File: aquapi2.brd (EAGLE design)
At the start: 102.5 x 80 mm, 4 parts, among them IC1 RASPBERRY_PI_ZERO_W__V1.3_

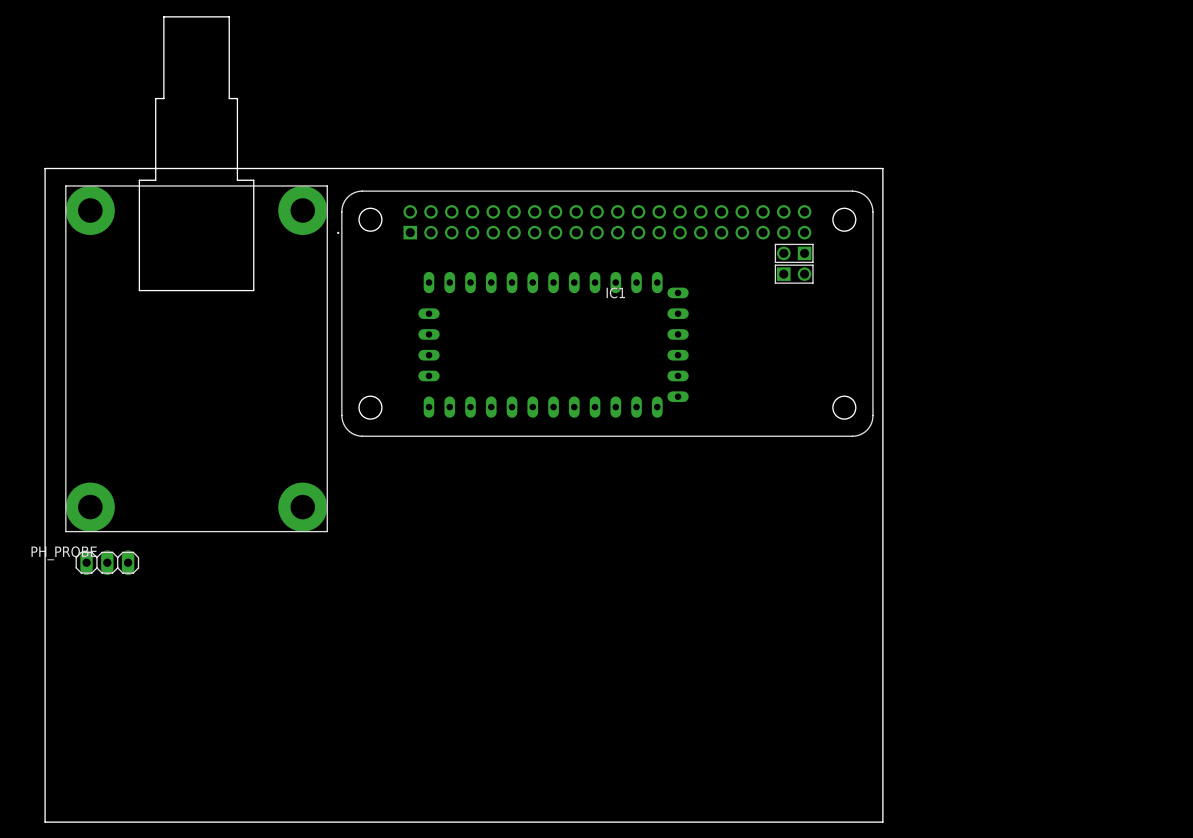
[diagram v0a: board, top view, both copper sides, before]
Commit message: relayx8 lib added
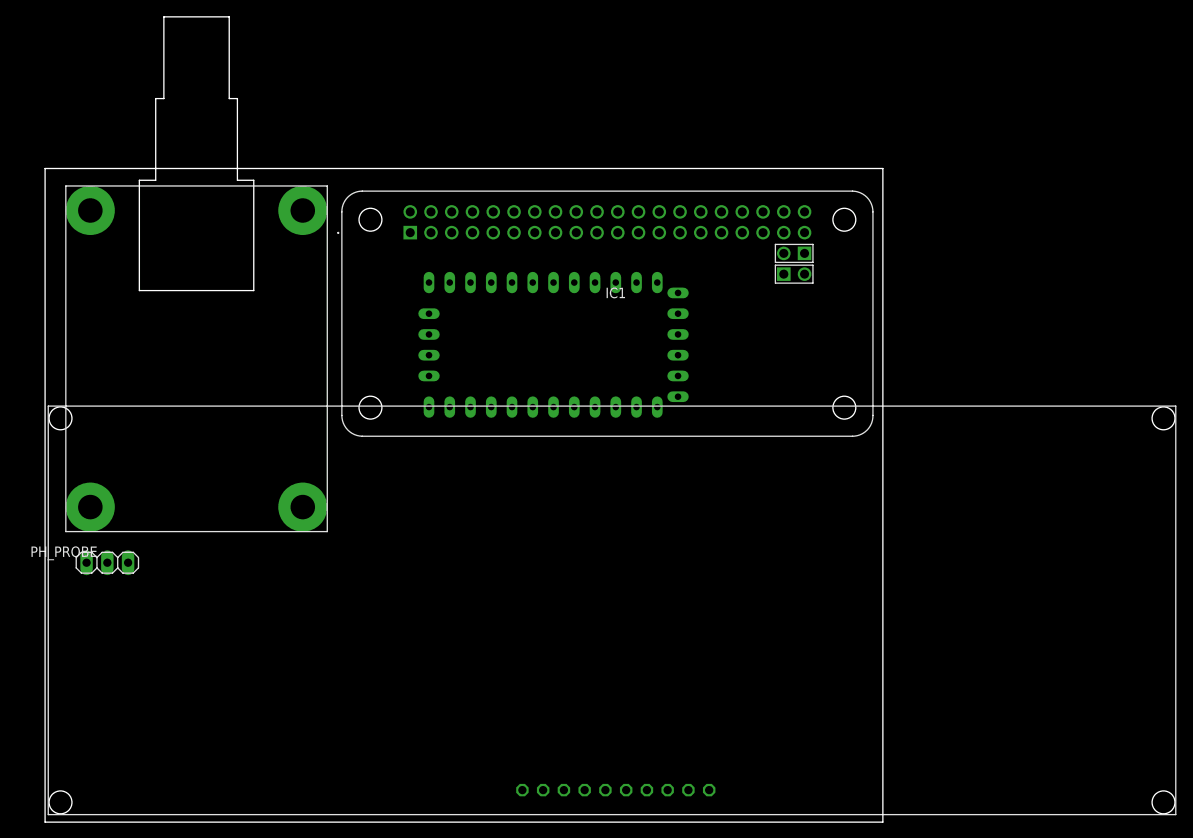
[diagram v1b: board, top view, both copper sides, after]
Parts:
- added U$3: RELAY_X8, RELAYx8:RELAY_X8
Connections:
- net +5V: now also U$3.VCC
- net GND: now also U$3.GND
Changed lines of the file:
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@@
 <setting verticaltext="up"/>
 </settings>
-<grid distance="50" unitdist="mil" unit="mil" style="lines" multiple="1" display="no" altdistance="5" altunitdist="mil" altunit="mil"/>
+<grid distance="1" unitdist="mm" unit="mm" style="lines" multiple="1" display="no" altdistance="1" altunitdist="mil" altunit="mm"/>
 <layers>
 <layer number="1" name="Top" color="4" fill="1" visible="yes" active="yes"/>
@@
 <attribute name="VALUE" x="11.43" y="34.925" size="1.27" layer="27" rot="R180"/>
 </element>
+<element name="U$3" library="RELAYx8" package="RELAY_X8" value="RELAY_X8" x="0.39" y="0.92" smashed="yes"/>
 </elements>
 <signals>
@@
 <contactref element="U$2" pad="GND"/>
 <contactref element="IC1" pad="14"/>
+<contactref element="U$3" pad="GND"/>
 <wire x1="85.335" y1="74.69" x2="92.955" y2="72.15" width="0" layer="19" extent="1-1"/>
 <wire x1="80.255" y1="74.69" x2="85.335" y2="74.69" width="0" layer="19" extent="1-1"/>
 <wire x1="75.175" y1="72.15" x2="80.255" y2="74.69" width="0" layer="19" extent="1-1"/>
+<wire x1="77.47" y1="64.77" x2="75.175" y2="72.15" width="0" layer="19" extent="1-1"/>
+<wire x1="77.47" y1="62.23" x2="77.47" y2="64.77" width="0" layer="19" extent="1-1"/>
 <wire x1="67.555" y1="74.69" x2="75.175" y2="72.15" width="0" layer="19" extent="1-1"/>
 <wire x1="59.935" y1="74.69" x2="67.555" y2="74.69" width="0" layer="19" extent="1-1"/>
-<wire x1="72.39" y1="50.8" x2="59.935" y2="74.69" width="0" layer="19" extent="1-1"/>
-<wire x1="77.47" y1="62.23" x2="72.39" y2="50.8" width="0" layer="19" extent="1-1"/>
-<wire x1="77.47" y1="64.77" x2="77.47" y2="62.23" width="0" layer="19" extent="1-1"/>
-<wire x1="67.31" y1="66.04" x2="77.47" y2="64.77" width="0" layer="19" extent="1-1"/>
-<wire x1="5.08" y1="31.75" x2="67.31" y2="66.04" width="0" layer="19" extent="1-1"/>
+<wire x1="67.31" y1="66.04" x2="67.555" y2="74.69" width="0" layer="19" extent="1-1"/>
+<wire x1="72.39" y1="50.8" x2="77.47" y2="62.23" width="0" layer="19" extent="1-1"/>
+<wire x1="5.08" y1="31.75" x2="59.935" y2="74.69" width="0" layer="19" extent="1-1"/>
+<wire x1="58.42" y1="3.92" x2="5.08" y2="31.75" width="0" layer="19" extent="1-1"/>
 </signal>
 <signal name="+5V">
@@
 <contactref element="IC1" pad="4"/>
 <contactref element="U$2" pad="VCC"/>
+<contactref element="U$3" pad="VCC"/>
 <wire x1="44.695" y1="74.69" x2="47.235" y2="74.69" width="0" layer="19" extent="1-1"/>
-<wire x1="67.31" y1="50.8" x2="44.695" y2="74.69" width="0" layer="19" extent="1-1"/>
-<wire x1="7.62" y1="31.75" x2="67.31" y2="50.8" width="0" layer="19" extent="1-1"/>
+<wire x1="67.31" y1="50.8" x2="47.235" y2="74.69" width="0" layer="19" extent="1-1"/>
+<wire x1="7.62" y1="31.75" x2="44.695" y2="74.69" width="0" layer="19" extent="1-1"/>
+<wire x1="81.28" y1="3.92" x2="7.62" y2="31.75" width="0" layer="19" extent="1-1"/>
 </signal>
 <signal name="ARD_RST">
